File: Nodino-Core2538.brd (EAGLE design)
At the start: 27.9 x 25.4 mm, 20 parts, among them CON1 NODINO-JTAGMODULE, CON2 USB-OTG_SHIELD, IC1 CC2538, IC2 AP733333SAG, Q1 32MHz, Q2 32.768kHz

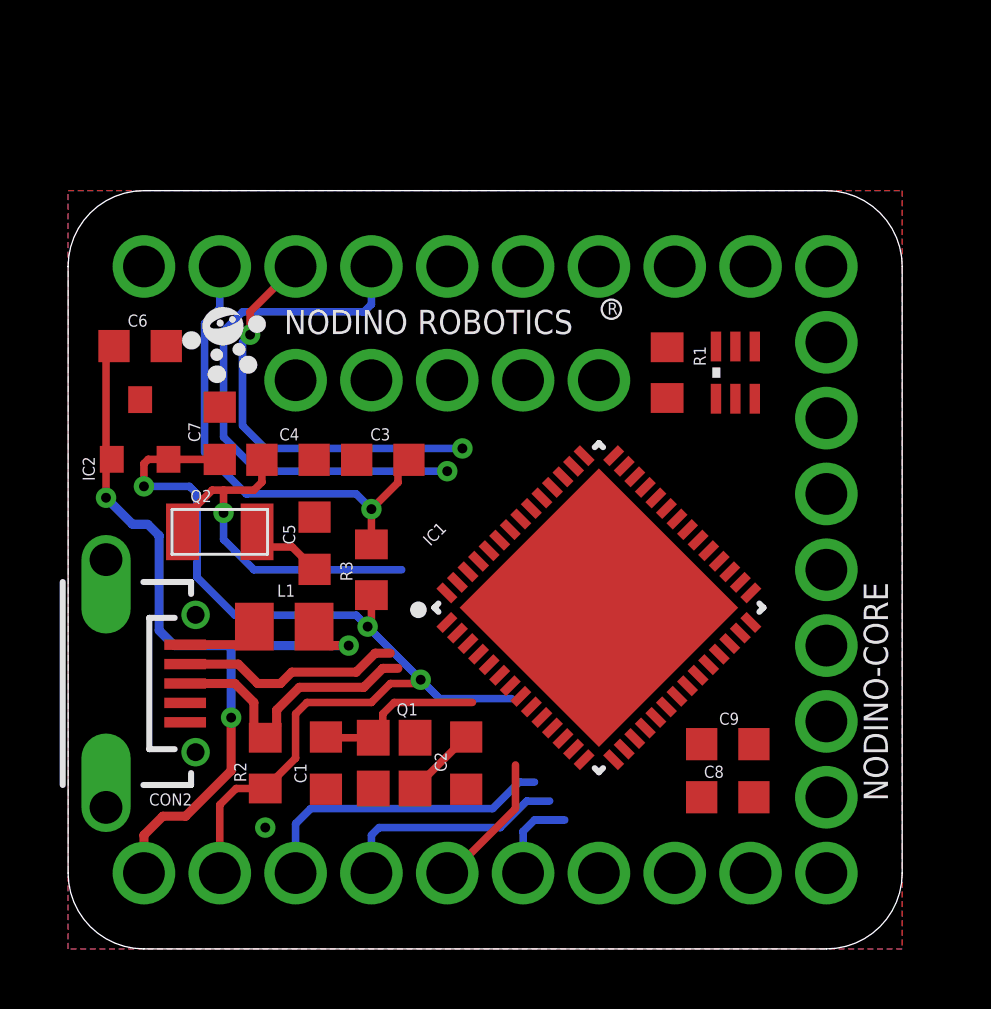
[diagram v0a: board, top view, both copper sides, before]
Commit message: almost done, but I think we need to remove the chip antenna
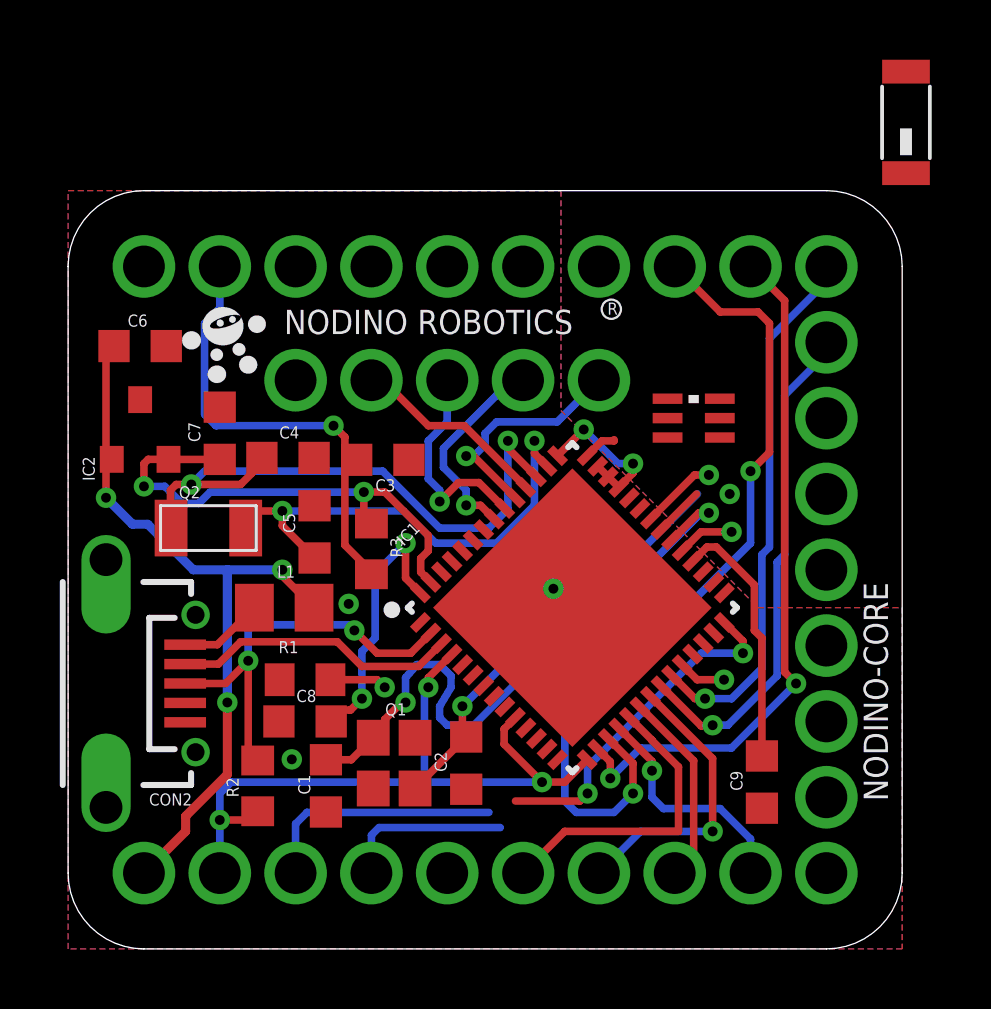
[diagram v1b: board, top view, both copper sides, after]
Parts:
- added ANT1: 2450AT18B100, johanson-technology:2450AT18B100
- moved R1 15.9 mm to (7.94, 9.02), turned to 0 degrees
- moved C8 14.4 mm to (7.94, 7.62), turned to 180 degrees
- moved F1 2.07 mm to (21.0, 17.8), turned to 270 degrees
- moved C9 1.71 mm to (23.2, 5.59), turned to 270 degrees
- moved IC1 0.89 mm to (16.9, 11.4)
- moved R2 0.80 mm to (6.35, 5.46)
- moved C1 0.76 mm to (8.64, 5.46)
- moved R3 0.70 mm to (10.2, 13.4), turned to 90 degrees
- moved L1 0.63 mm to (7.24, 11.4)
- moved Q2 0.40 mm to (4.70, 14.1)
- moved C5 0.38 mm to (8.26, 14.0)
- moved C4 0.06 mm to (7.37, 16.4)
- turned C3 to 0 degrees
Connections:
- net WKUP renamed CS3
- removed net CAN_RX: CON1.22
- removed net CAN_TX: CON1.21
- removed net I2C1_SCL: CON1.24
- removed net I2C1_SDA: CON1.23
- removed net I2C1_SMBA: CON1.25
- removed net N$10: IC1.52
- removed net N$11: IC1.53
- removed net N$12: IC1.54
- removed net N$13: IC1.5
- removed net N$14: IC1.23
- removed net N$15: IC1.22
- removed net N$16: IC1.21
- removed net N$17: IC1.20
- removed net N$18: IC1.19
- removed net N$19: IC1.18
- removed net N$22: IC1.14
- removed net N$23: IC1.13
- removed net N$24: IC1.12
- removed net N$25: IC1.11
- removed net N$26: IC1.9
- removed net N$27: IC1.8
- removed net N$28: IC1.7
- removed net N$29: IC1.6
- removed net N$30: IC1.25
- removed net N$31: IC1.26
- removed net N$32: IC1.27
- removed net N$33: IC1.29
- removed net N$34: IC1.30
- removed net N$6: IC1.50
- removed net N$9: IC1.51
- removed net SDADC1_4P: CON1.13
- removed net SDADC1_5P: CON1.12
- removed net SDADC1_6P: CON1.11
- removed net SDADC1_7P: CON1.15
- removed net SDADC1_8P: CON1.14
- removed net SDADC3_6P: CON1.18
- removed net SDADC3_7P: CON1.17
- removed net SDADC3_8P: CON1.16
- removed net SPI3_MISO: CON1.8
- removed net SPI3_MOSI: CON1.7
- removed net SPI3_NSS: CON1.6
- removed net SPI3_SCK: CON1.9
- removed net VREFSD+: CON1.10
- new net PA6: CON1.17, IC1.22
- new net PA7: CON1.18, IC1.23
- new net SPI_MISO: CON1.8, IC1.20
- new net SPI_MOSI: CON1.7, IC1.21
- new net SPI_NSS: CON1.6, IC1.19
- new net SPI_SCK: CON1.9, IC1.18
- net N$2: now also ANT1.1
- net RF_N: now also F1.3; no longer F1.4
- net RF_P: now also F1.4; no longer F1.3
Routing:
- net UART_TX: track 0.00 -> 27.7 mm, vias 0 -> 2
- net UART_RX: track 0.00 -> 23.3 mm, vias 0 -> 2
- net +3V3: track 33.1 -> 52.7 mm, vias 3 -> 10
- net PA7: track 0.00 -> 18.1 mm, vias 0 -> 1
- net I2C1_SCL: track 18.1 -> 0.00 mm, vias 1 -> 0
- net PA6: track 0.00 -> 17.0 mm, vias 0 -> 1
- net N$8: track 5.68 -> 21.5 mm, vias 0 -> 2
- net 32K1: track 2.51 -> 17.0 mm, vias 0 -> 2
- net I2C1_SMBA: track 13.8 -> 0.00 mm, vias 2 -> 0
- net N$7: track 2.43 -> 16.0 mm, vias 0 -> 2
- net NRST: track 16.2 -> 27.0 mm, vias 1 -> 3
- net SPI_NSS: track 0.00 -> 10.3 mm
- net SPI_MOSI: track 0.00 -> 9.77 mm, vias 0 -> 1
- net N$3: track 0.00 -> 9.03 mm, vias 0 -> 2
- net N$4: track 0.00 -> 8.62 mm
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
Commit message: all connected, except CC2538 ground pad and balun
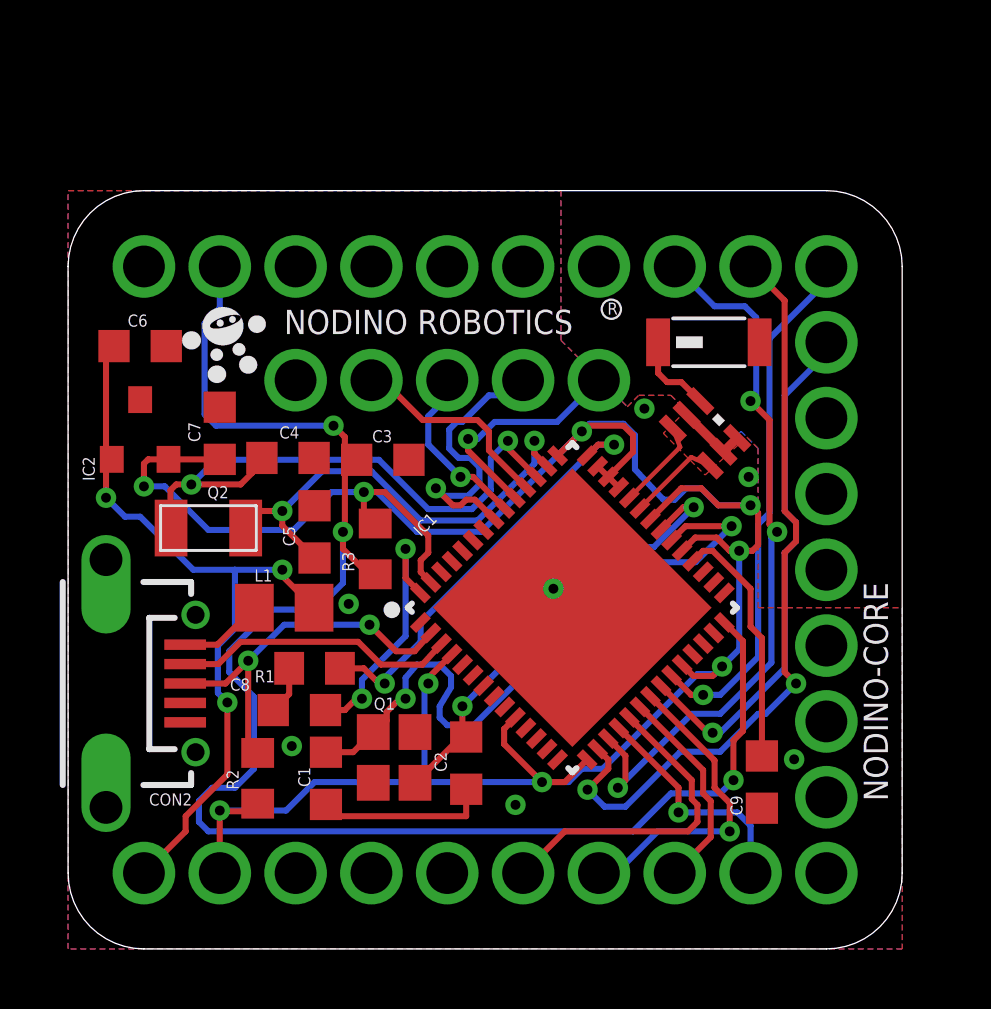
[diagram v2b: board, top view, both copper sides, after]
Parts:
- moved ANT1 9.89 mm to (21.5, 20.3), turned to 0 degrees
- moved F1 0.64 mm to (21.3, 17.3), turned to 225 degrees
- moved R1 0.50 mm to (8.26, 9.40)
- moved C8 0.43 mm to (7.75, 8.00)
- moved C1 0.25 mm to (8.64, 5.71)
- moved R2 0.25 mm to (6.35, 5.71)
- moved Q1 0.19 mm to (10.9, 6.41)
- moved R3 0.13 mm to (10.3, 13.4)
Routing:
- net +3V3: track 52.7 -> 86.5 mm, vias 10 -> 9
- net NRST: track 27.0 -> 53.9 mm
- net N$5: track 3.07 -> 14.3 mm, vias 1 -> 2
- net GND: track 0.00 -> 9.78 mm, vias 3 -> 7
- net CS1: track 8.29 -> 0.00 mm
- net CS2: track 5.69 -> 0.00 mm
- net UART_TX: track 27.7 -> 24.4 mm, vias 2 -> 3
- net RF_P: track 0.00 -> 3.11 mm
- net RF_N: track 0.00 -> 3.07 mm
- net JTDI: track 6.96 -> 9.91 mm
- net N$2: track 0.00 -> 2.83 mm
- net UART_RX: track 23.3 -> 25.6 mm
- net JTDO: track 7.29 -> 5.87 mm
- net N$8: track 21.5 -> 22.5 mm
- net 32K2: track 20.6 -> 19.7 mm
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
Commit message: all done! but need to check and double check again before fab
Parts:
- moved C5 0.06 mm to (8.19, 14.0)
- moved L1 0.06 mm to (7.18, 11.4)
- moved R3 0.06 mm to (10.4, 13.4)
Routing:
- net GND: track 9.78 -> 15.1 mm, vias 7 -> 8
- net N$7: track 15.3 -> 20.3 mm
- net NRST: track 53.9 -> 55.1 mm
- net +3V3: track 86.5 -> 87.5 mm
- net N$8: track 22.5 -> 21.6 mm

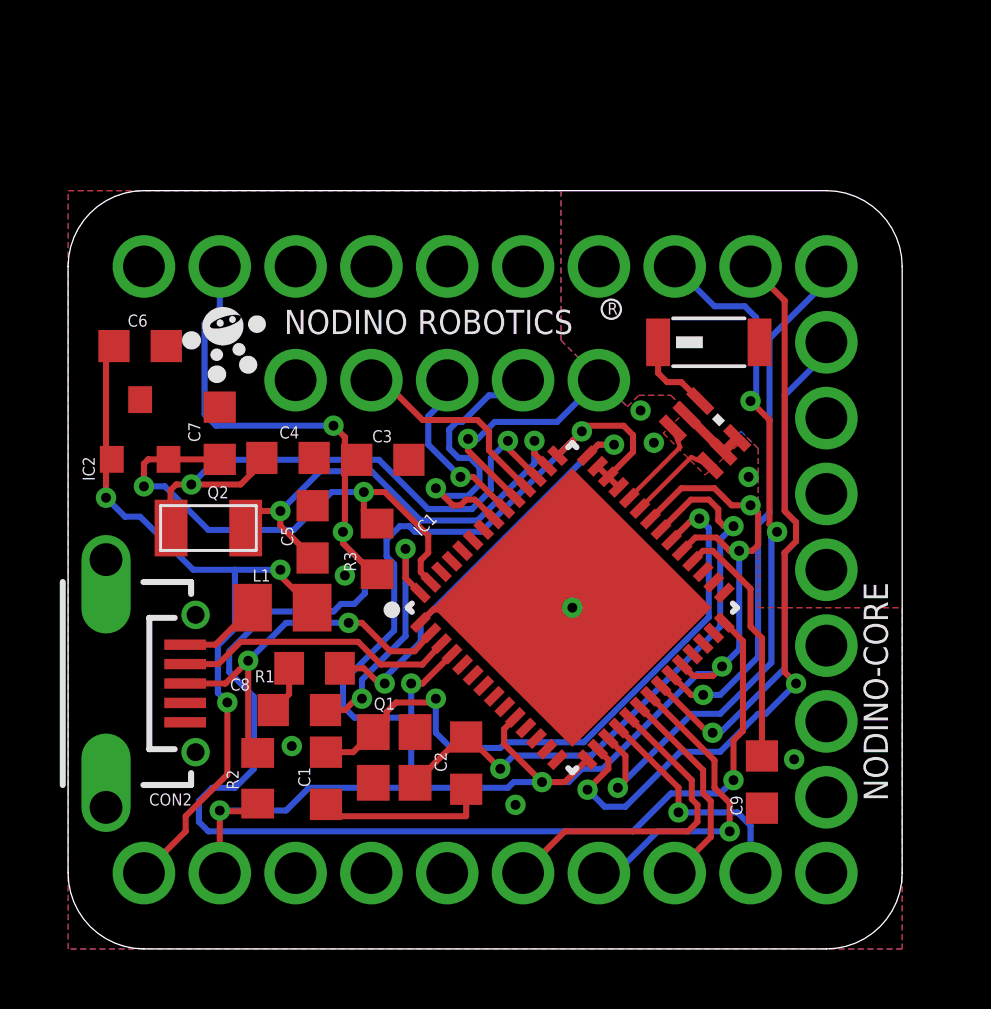
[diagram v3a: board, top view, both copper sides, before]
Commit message: added CS1, CS2, CS3
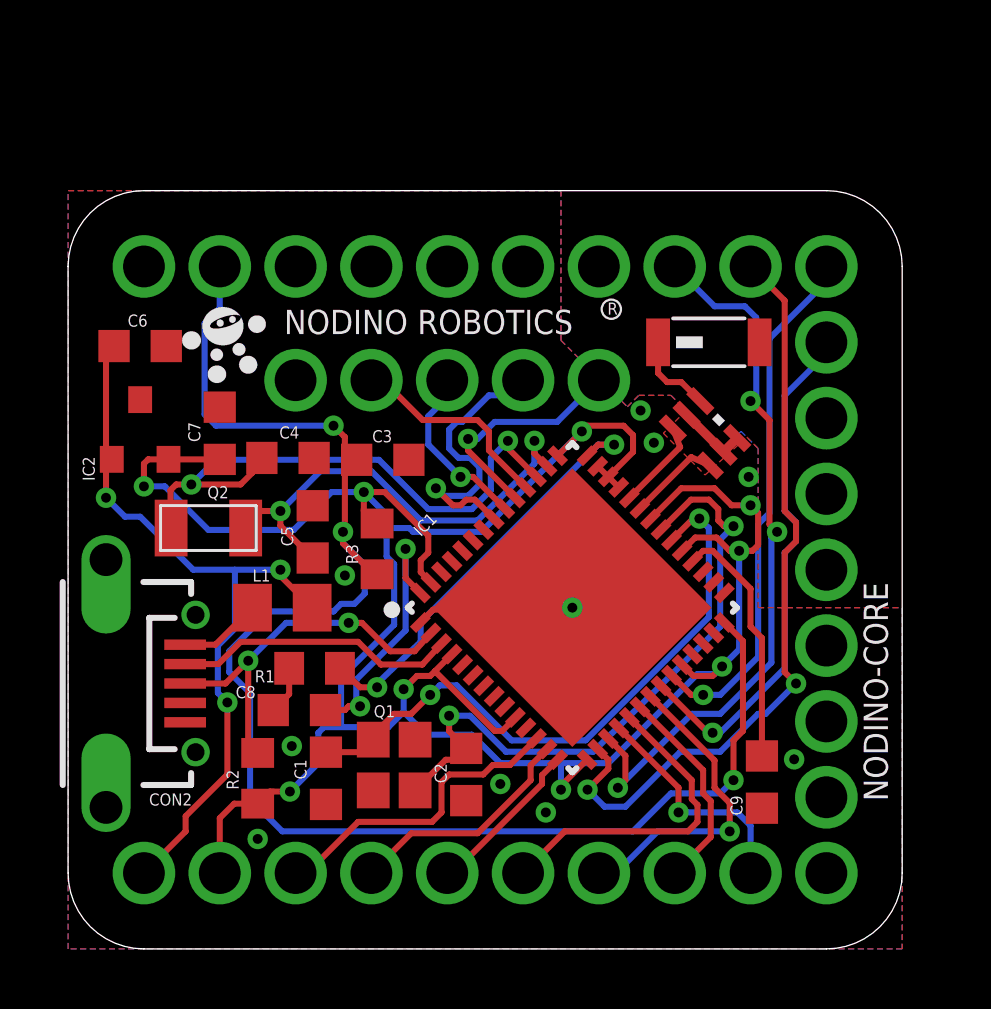
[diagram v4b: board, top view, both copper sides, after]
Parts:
- moved C2 0.38 mm to (13.3, 5.84)
- moved Q1 0.25 mm to (10.9, 6.16)
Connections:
- net CS1: now also IC1.12
- net CS2: now also IC1.13
- net CS3: now also IC1.14
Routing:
- net CS1: track 0.00 -> 10.5 mm
- net CS2: track 0.00 -> 7.89 mm
- net GND: track 15.1 -> 9.31 mm, vias 8 -> 10
- net CS3: track 0.00 -> 5.44 mm
- net NRST: track 55.1 -> 51.6 mm
- net N$7: track 20.3 -> 21.9 mm
- net +3V3: track 87.5 -> 86.4 mm
- net N$8: track 21.6 -> 21.0 mm

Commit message: added D2-D6
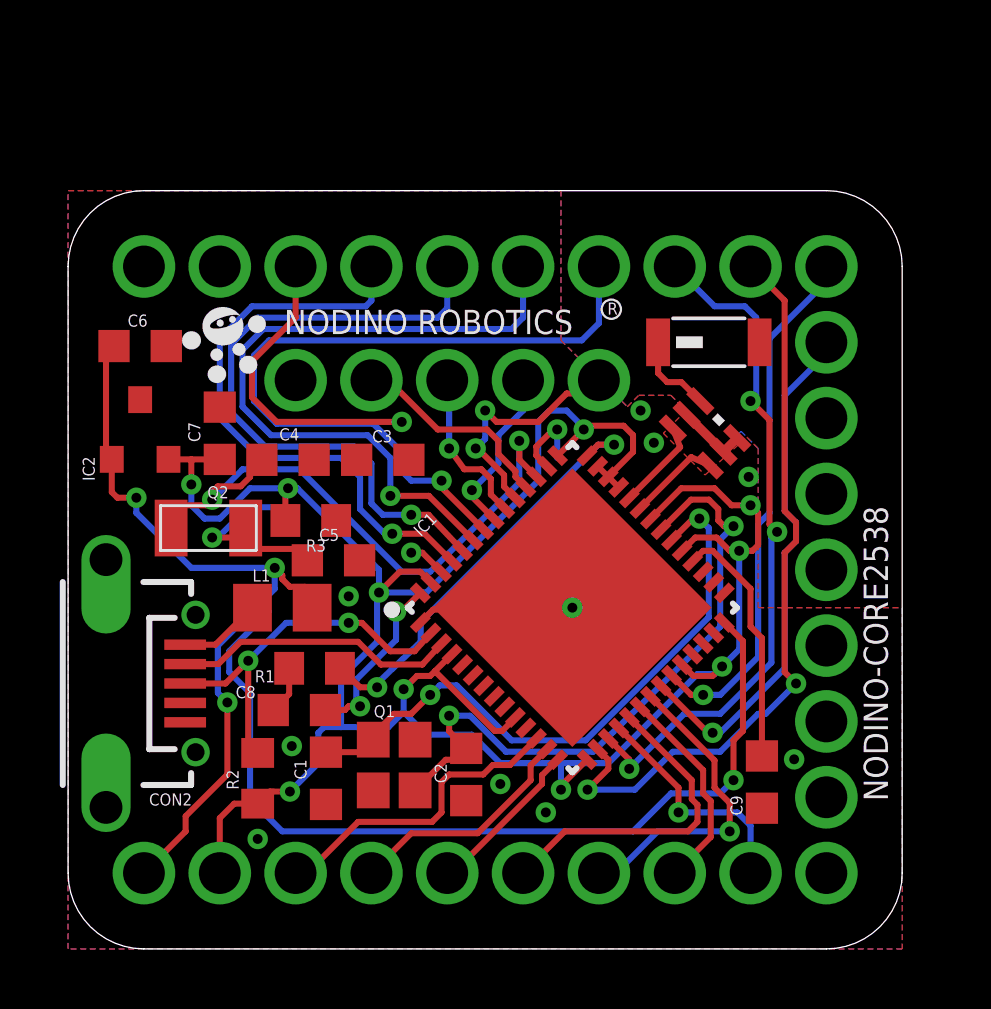
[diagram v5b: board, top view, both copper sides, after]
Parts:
- moved R3 2.42 mm to (8.13, 14.4), turned to 180 degrees
- moved C5 1.18 mm to (8.89, 13.0), turned to 0 degrees
- moved C4 0.06 mm to (7.37, 16.4)
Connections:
- new net PB1: CON1.25, IC1.54
- new net PB2: CON1.24, IC1.53
- new net PB3: CON1.23, IC1.52
- new net PB4: CON1.22, IC1.51
- new net PB5: CON1.21, IC1.50
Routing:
- net PB5: track 0.00 -> 25.4 mm, vias 0 -> 1
- net PB4: track 0.00 -> 23.8 mm, vias 0 -> 1
- net PB3: track 0.00 -> 21.9 mm, vias 0 -> 1
- net NRST: track 51.6 -> 30.2 mm, vias 3 -> 1
- net PB2: track 0.00 -> 19.8 mm, vias 0 -> 1
- net PB1: track 0.00 -> 11.6 mm, vias 0 -> 2
- net 32K1: track 16.7 -> 10.6 mm
- net JTDI: track 9.91 -> 5.67 mm
- net +3V3: track 86.4 -> 82.9 mm, vias 9 -> 10
- net N$3: track 8.90 -> 6.06 mm
- net UART_TX: track 24.4 -> 23.1 mm
- net 32K2: track 19.7 -> 20.9 mm
- net +5V: track 25.6 -> 26.3 mm
- net JTCK: track 7.83 -> 8.19 mm, vias 1 -> 2
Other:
- board text added: "NODINO-CORE2538"
- board text removed: "NODINO-CORE"

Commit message: update for D2-D6
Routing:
- net NRST: track 30.2 -> 57.1 mm, vias 1 -> 4
- net 32K1: track 10.6 -> 21.4 mm
- net 32K2: track 20.9 -> 27.5 mm
- net PB1: track 11.6 -> 17.5 mm
- net PB2: track 19.8 -> 21.4 mm
- net PB3: track 21.9 -> 23.4 mm
- net +5V: track 26.3 -> 27.4 mm
- net PB4: track 23.8 -> 23.0 mm
- net PB5: track 25.4 -> 24.9 mm
- net GND: vias 10 -> 9
